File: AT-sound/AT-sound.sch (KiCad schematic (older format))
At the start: 28 parts, among them J1 PWR, J2 Sound OUT, J3 Sound IN, J4 PWR, U1 ATtiny24-20SSU

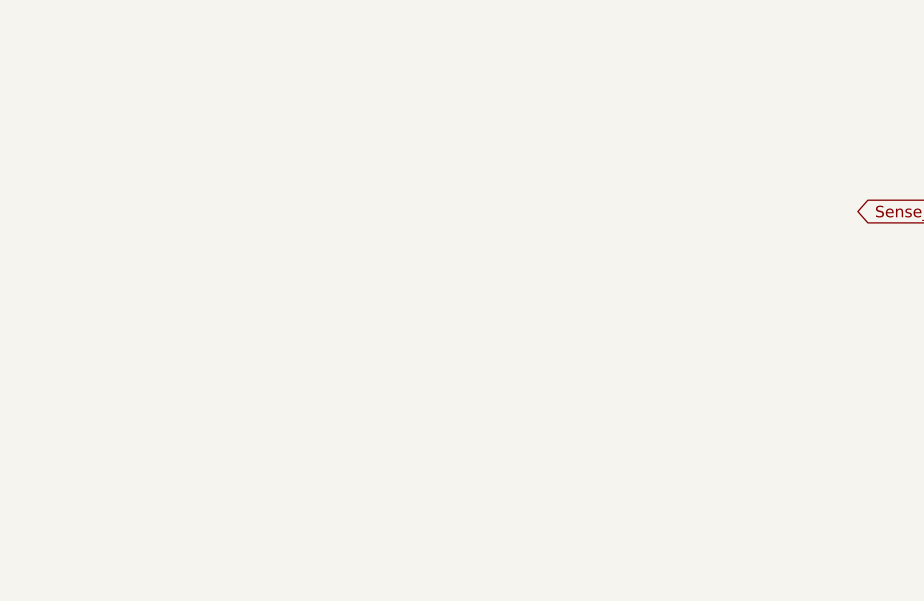
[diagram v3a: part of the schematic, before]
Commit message: added capacitive dropper cirict for POWERgit add *git add *git add *
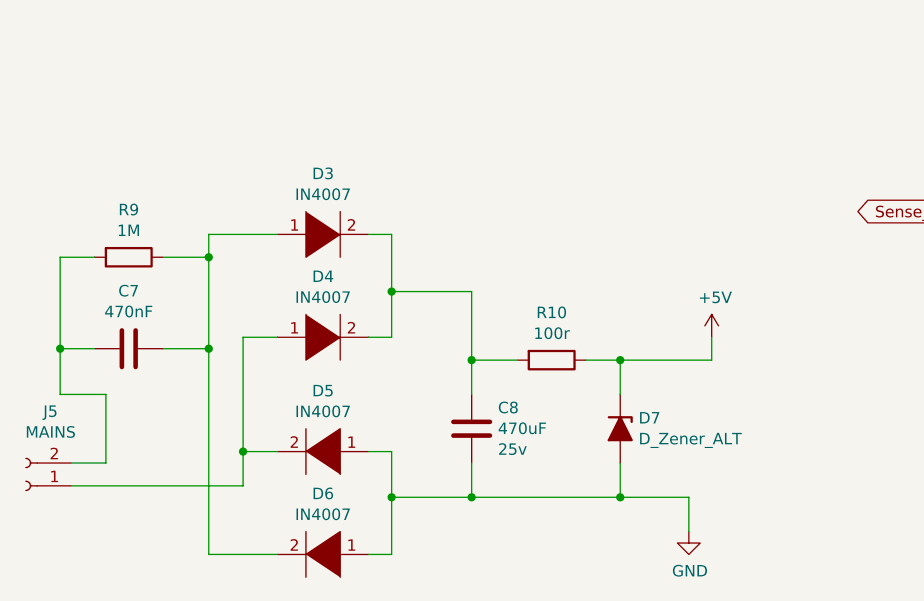
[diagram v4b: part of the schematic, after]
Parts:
- added C7: 470nF, Capacitor_THT:C_Radial_D12.5mm_H25.0mm_P5.00mm, symbol Device:C
- added C8: 470uF, Capacitor_THT:C_Radial_D6.3mm_H5.0mm_P2.50mm, symbol Device:C
- added D3, D4, D5, D6: IN4007, Diode_THT:D_A-405_P10.16mm_Horizontal, symbol pspice:DIODE
- added D7: D_Zener_ALT, Diode_THT:D_T-1_P5.08mm_Horizontal, symbol Device:D_Zener_ALT
- added J5: MAINS, Connector_PinSocket_2.54mm:PinSocket_1x02_P2.54mm_Vertical, symbol Connector:Conn_01x02_Female
- added R10: 100r, Resistor_THT:R_Axial_DIN0207_L6.3mm_D2.5mm_P7.62mm_Horizontal, symbol Device:R
- added R9: 1M, Resistor_THT:R_Axial_DIN0207_L6.3mm_D2.5mm_P7.62mm_Horizontal, symbol Device:R
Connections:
- net +5V: now also D7.1 (K), R10.1
- net GND: now also C8.1, D5.1 (K), D6.1 (K), D7.2 (A)
- new net: C7.1, D3.1 (K), D6.2 (A), R9.1
- new net: C8.2, D3.2 (A), D4.2 (A), R10.2
- new net: D4.1 (K), D5.2 (A), J5.1 (Pin_1)
- new net: C7.2, J5.2 (Pin_2), R9.2
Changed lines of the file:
@@
 Wire Wire Line
 	9850 5500 9850 5400
+$Comp
+L pspice:DIODE D3
+U 1 1 609AD9BF
+P 2000 6150
+F 0 "D3" H 2000 6415 50  0000 C CNN
+F 1 "IN4007" H 2000 6324 50  0000 C CNN
+F 2 "Diode_THT:D_A-405_P10.16mm_Horizontal" H 2000 6150 50  0001 C CNN
+F 3 "~" H 2000 6150 50  0001 C CNN
+	1    2000 6150
+	1    0    0    -1
+$EndComp
+$Comp
+L pspice:DIODE D4
+U 1 1 609ADDC7
+P 2000 6600
+F 0 "D4" H 2000 6865 50  0000 C CNN
+F 1 "IN4007" H 2000 6774 50  0000 C CNN
+F 2 "Diode_THT:D_A-405_P10.16mm_Horizontal" H 2000 6600 50  0001 C CNN
+F 3 "~" H 2000 6600 50  0001 C CNN
+	1    2000 6600
+	1    0    0    -1
+$EndComp
+$Comp
+L pspice:DIODE D5
+U 1 1 609AE1D2
+P 2000 7100
+F 0 "D5" H 2000 6835 50  0000 C CNN
+F 1 "IN4007" H 2000 6926 50  0000 C CNN
+F 2 "Diode_THT:D_A-405_P10.16mm_Horizontal" H 2000 7100 50  0001 C CNN
+F 3 "~" H 2000 7100 50  0001 C CNN
+	1    2000 7100
+	-1   0    0    1
+$EndComp
+$Comp
+L pspice:DIODE D6
+U 1 1 609AE84E
+P 2000 7550
+F 0 "D6" H 2000 7285 50  0000 C CNN
+F 1 "IN4007" H 2000 7376 50  0000 C CNN
+F 2 "Diode_THT:D_A-405_P10.16mm_Horizontal" H 2000 7550 50  0001 C CNN
+F 3 "~" H 2000 7550 50  0001 C CNN
+	1    2000 7550
+	-1   0    0    1
+$EndComp
+$Comp
+L Device:C C7
+U 1 1 609AF0FC
+P 1150 6650
+F 0 "C7" V 898 6650 50  0000 C CNN
+F 1 "470nF" V 989 6650 50  0000 C CNN
+F 2 "Capacitor_THT:C_Radial_D12.5mm_H25.0mm_P5.00mm" H 1188 6500 50  0001 C CNN
+F 3 "~" H 1150 6650 50  0001 C CNN
+	1    1150 6650
+	0    1    1    0
+$EndComp
+$Comp
+L Device:R R9
+U 1 1 609AF90D
+P 1150 6250
+F 0 "R9" V 943 6250 50  0000 C CNN
+F 1 "1M" V 1034 6250 50  0000 C CNN
+F 2 "Resistor_THT:R_Axial_DIN0207_L6.3mm_D2.5mm_P7.62mm_Horizontal" V 1080 6250 50  0001 C CNN
+F 3 "~" H 1150 6250 50  0001 C CNN
+	1    1150 6250
+	0    1    1    0
+$EndComp
+$Comp
+L Device:C C8
+U 1 1 609B1668
+P 2650 7000
+F 0 "C8" H 2535 6909 50  0000 R CNN
+F 1 "470uF" H 2535 7000 50  0000 R CNN
+F 2 "Capacitor_THT:C_Radial_D6.3mm_H5.0mm_P2.50mm" H 2688 6850 50  0001 C CNN
+F 3 "~" H 2650 7000 50  0001 C CNN
+F 4 "25v" H 2535 7091 50  0000 R CNN "Voltage rating"
+	1    2650 7000
+	-1   0    0    1
+$EndComp
+$Comp
+L Device:R R10
+U 1 1 609B166E
+P 3000 6700
+F 0 "R10" V 2793 6700 50  0000 C CNN
+F 1 "100r" V 2884 6700 50  0000 C CNN
+F 2 "Resistor_THT:R_Axial_DIN0207_L6.3mm_D2.5mm_P7.62mm_Horizontal" V 2930 6700 50  0001 C CNN
+F 3 "~" H 3000 6700 50  0001 C CNN
+	1    3000 6700
+	0    1    1    0
+$EndComp
+$Comp
+L Device:D_Zener_ALT D7
+U 1 1 609B7172
+P 3300 7000
+F 0 "D7" V 3254 7080 50  0000 L CNN
+F 1 "D_Zener_ALT" V 3345 7080 50  0000 L CNN
+F 2 "Diode_THT:D_T-1_P5.08mm_Horizontal" H 3300 7000 50  0001 C CNN
+F 3 "~" H 3300 7000 50  0001 C CNN
+	1    3300 7000
+	0    1    1    0
+$EndComp
+Wire Wire Line
+	2200 6150 2300 6150
+Wire Wire Line
+	2300 6150 2300 6400
+Wire Wire Line
+	2300 6600 2200 6600
+Wire Wire Line
+	2200 7100 2300 7100
+Wire Wire Line
+	2300 7100 2300 7300
+Wire Wire Line
+	2300 7550 2200 7550
+Wire Wire Line
+	2300 7300 2650 7300
+Wire Wire Line
+	3300 7300 3300 7150
+Connection ~ 2300 7300
+Wire Wire Line
+	2300 7300 2300 7550
+Wire Wire Line
+	2650 7150 2650 7300
+Connection ~ 2650 7300
+Wire Wire Line
+	2650 7300 3300 7300
+Wire Wire Line
+	1800 7100 1650 7100
+Wire Wire Line
+	1650 7100 1650 6600
+Wire Wire Line
+	1650 6600 1800 6600
+Wire Wire Line
+	1800 6150 1500 6150
+Wire Wire Line
+	1500 6150 1500 6250
+Wire Wire Line
+	1500 7550 1800 7550
+Wire Wire Line
+	2650 6850 2650 6700
+Wire Wire Line
+	2650 6400 2300 6400
+Connection ~ 2300 6400
+Wire Wire Line
+	2300 6400 2300 6600
+Wire Wire Line
+	2850 6700 2650 6700
+Connection ~ 2650 6700
+Wire Wire Line
+	2650 6700 2650 6400
+Wire Wire Line
+	3150 6700 3300 6700
+Wire Wire Line
+	3300 6700 3300 6850
+Wire Wire Line
+	3300 6700 3700 6700
+Wire Wire Line
+	3700 6700 3700 6600
+Connection ~ 3300 6700
+$Comp
+L power:+5V #PWR0106
+U 1 1 609E20EC
+P 3700 6600
+F 0 "#PWR0106" H 3700 6450 50  0001 C CNN
+F 1 "+5V" H 3715 6773 50  0000 C CNN
+F 2 "" H 3700 6600 50  0001 C CNN
+F 3 "" H 3700 6600 50  0001 C CNN
+	1    3700 6600
+	1    0    0    -1
+$EndComp
+$Comp
+L power:GND #PWR0113
+U 1 1 609E271E
+P 3600 7450
+F 0 "#PWR0113" H 3600 7200 50  0001 C CNN
+F 1 "GND" H 3605 7277 50  0000 C CNN
+F 2 "" H 3600 7450 50  0001 C CNN
+F 3 "" H 3600 7450 50  0001 C CNN
+	1    3600 7450
+	1    0    0    -1
+$EndComp
+Wire Wire Line
+	3300 7300 3600 7300
+Wire Wire Line
+	3600 7300 3600 7450
+Connection ~ 3300 7300
+Wire Wire Line
+	1300 6250 1500 6250
+Connection ~ 1500 6250
+Wire Wire Line
+	1500 6250 1500 6650
+Wire Wire Line
+	1000 6250 850  6250
+Wire Wire Line
+	850  6250 850  6650
+Wire Wire Line
+	850  6650 1000 6650
+Wire Wire Line
+	1300 6650 1500 6650
+Connection ~ 1500 6650
+Wire Wire Line
+	1500 6650 1500 7550
+$Comp
+L Connector:Conn_01x02_Female J5
+U 1 1 609FB20D
+P 700 7250
+F 0 "J5" H 592 6925 50  0000 C CNN
+F 1 "MAINS" H 592 7016 50  0000 C CNN
+F 2 "Connector_PinSocket_2.54mm:PinSocket_1x02_P2.54mm_Vertical" H 700 7250 50  0001 C CNN
+F 3 "~" H 700 7250 50  0001 C CNN
+	1    700  7250
+	-1   0    0    1
+$EndComp
+Wire Wire Line
+	900  7150 1050 7150
+Wire Wire Line
+	1050 7150 1050 6850
+Wire Wire Line
+	1050 6850 850  6850
+Wire Wire Line
+	850  6850 850  6650
+Connection ~ 850  6650
+Wire Wire Line
+	900  7250 1650 7250
+Wire Wire Line
+	1650 7250 1650 7100
+Connection ~ 1650 7100
 $EndSCHEMATC
